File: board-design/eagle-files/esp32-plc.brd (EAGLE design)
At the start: 100 x 80 mm, 42 parts, among them P1 47346-0001, Q1 600mA/40V, Q2 600mA/40V, U1 ESP32-WROOM-32D, U2 FT231XS, U3 BD48E27G-TR, U5 EC20CEFASG-MINIPCIE

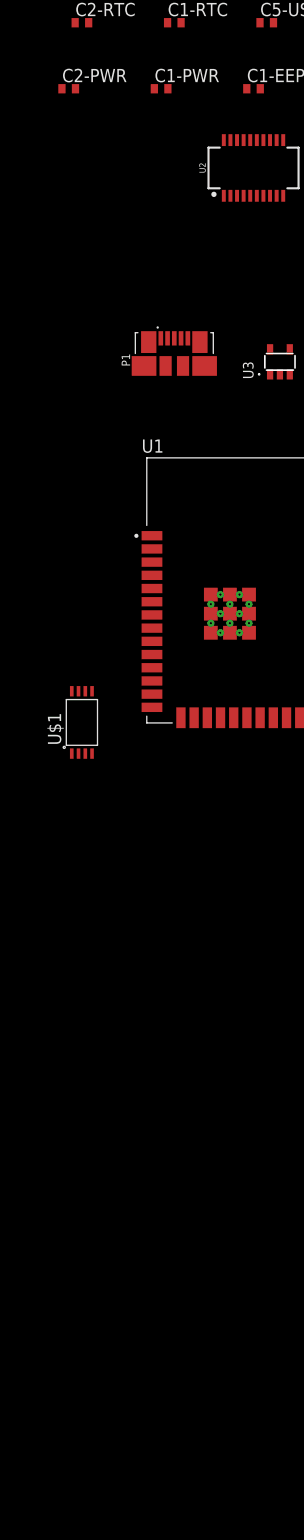
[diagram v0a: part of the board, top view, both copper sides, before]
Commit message: Changed board schematic
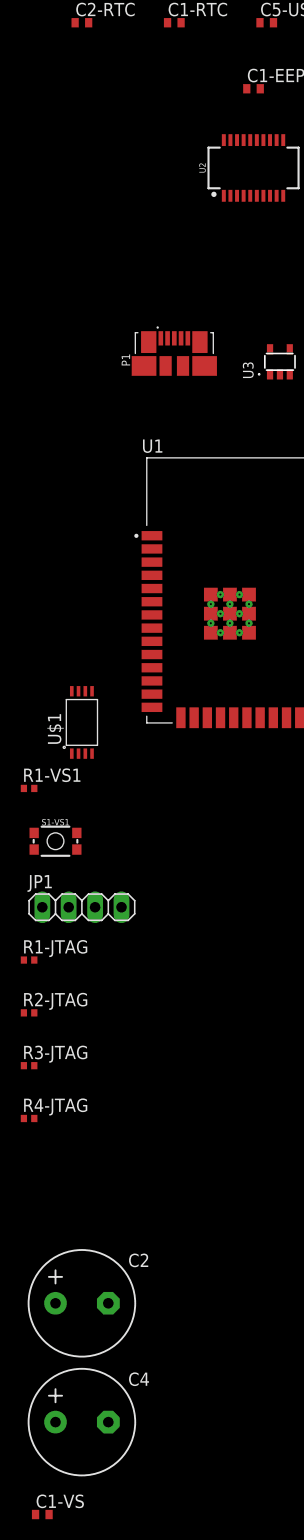
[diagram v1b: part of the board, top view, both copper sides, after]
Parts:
- removed C1-PWR: 100uF, rcl:C0402
- removed C2-PWR: 1000uF, rcl:C0402
- added C1-VS: 47pF, rcl:C0402
- added C2: 1000uF, cap-pan40:E5,0-10
- added C4: 100uF, cap-pan40:E5,0-10
- added JP1: (no value), pinhead:1X04
- added R1-JTAG, R2-JTAG, R3-JTAG, R4-JTAG: 100, rcl:R0402
- added R1-VS1: 10k, rcl:R0402
- added S1-VS1: (no value), SparkFun-Switches:TACTILE_SWITCH_SMD_4.6X2.8MM
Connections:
- net N$14 renamed STATUS
- net N$15 renamed VBAT_BB
- net N$16 renamed VBAT_RF
- net N$17 renamed ANT_DIV
- net N$18 renamed ANT_MAIN
- net N$19 renamed ANT_GNSS
- net N$2 renamed USB_VBUS
- net N$20 renamed ADC0
- net N$21 renamed ADC1
- net N$22 renamed I2C_SDA
- net N$23 renamed I2C_SCL
- net N$24 renamed VDD_EXT
- net N$25 renamed AP_READY
- net N$26 renamed W_DISABLE#
- net N$27 renamed NET_MODE
- net N$28 renamed NET_STATUS
- net N$39 renamed WAKEUP_IN
- net N$40 renamed DBG_RXD
- net N$41 renamed DBG_TXD
- net N$42 renamed USIM_VDD
- net N$43 renamed USIM_GND
- net N$44 renamed USIM_DATA
- net N$45 renamed USIM_CLK
- net N$46 renamed USIM_RST
- net N$47 renamed RESET_IN
- net N$48 renamed PWRKEY
- net N$49 renamed PCM_IN
- net N$5 renamed USB_DM
- net N$50 renamed PCM_OUT
- net N$51 renamed PCM_SYNC
- net N$52 renamed PCM_CLK
- net N$53 renamed RESERVED
- net N$6 renamed USB_DP
- removed net IO18: U1.30
- removed net IO19: U1.31
- removed net IO21: U1.33
- removed net IO22: U1.36
- removed net IO23: U1.37
- removed net IO25: U1.10
- removed net IO26: U1.11
- removed net IO27: U1.12
- removed net IO5: U1.29
- removed net N$54: U5.100, U5.101, U5.102, U5.103, U5.104, U5.105, U5.106, U5.107, U5.108, U5.109, U5.110, U5.111, U5.112, U5.19, U5.22, U5.36, U5.46, U5.48, U5.50, U5.51, U5.52, U5.53, U5.54, U5.56, U5.72, U5.8, U5.85, U5.86, U5.87, U5.88, U5.89, U5.9, U5.90, U5.91, U5.92, U5.93, U5.94, U5.95, U5.96, U5.97, U5.98, U5.99
- new net MTCK: JP1.3, R3-JTAG.2
- new net MTDI: JP1.2, R2-JTAG.2
- new net MTDO: JP1.4, R4-JTAG.2
- new net MTMS: JP1.1, R1-JTAG.2
- new net VIN: C4.+, U$2.1
- net 3V3: now also C1-VS.1, C2.+, R1-VS1.2; no longer C2-PWR.1
- net EEPROM_CLK: now also U1.30
- net EEPROM_CS: now also U1.29
- net EEPROM_DI: now also U1.37
- net EEPROM_DO: now also U1.31
- net EEPROM_HD: now also U1.33
- net EEPROM_WP: now also U1.36
- net GND: now also C1-VS.2, C2.-, C4.-, S1-VS1.3, S1-VS1.4, U5.100, U5.101, U5.102, U5.103, U5.104, U5.105, U5.106, U5.107, U5.108, U5.109, U5.110, U5.111, U5.112, U5.19, U5.22, U5.36, U5.46, U5.48, U5.50, U5.51, U5.52, U5.53, U5.54, U5.56, U5.72, U5.8, U5.85, U5.86, U5.87, U5.88, U5.89, U5.9, U5.90, U5.91, U5.92, U5.93, U5.94, U5.95, U5.96, U5.97, U5.98, U5.99; no longer C1-PWR.2, C2-PWR.2
- net IO0: no longer U1.25
- net IO12: now also R2-JTAG.1
- net IO13: now also R3-JTAG.1
- net IO14: now also R1-JTAG.1
- net IO15: now also R4-JTAG.1
- net N$1: now also R1-VS1.1, S1-VS1.1, S1-VS1.2, U1.25; no longer C1-PWR.1, U$2.1
- net RTC_MFP: now also U1.12
- net SCL: now also U1.10
- net SDA: now also U1.11

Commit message: Eagle schematic changed
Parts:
- removed C1-ESP: 1uF, rcl:C0402
- removed C1-RTC, C2-RTC: 5pF, rcl:C0402
- removed C1-USB, C3, C3-ESP: 0.1uF, rcl:C0402
- removed C2: 1000uF, cap-pan40:E5,0-10
- removed C2-ESP: 10uF, rcl:C0402
- removed C2-USB: 4.7uF, rcl:C0402
- removed C3-USB, C4-USB: 47pF, rcl:C0402
- removed C4: 100uF, cap-pan40:E5,0-10
- removed C5-USB: 10nF, rcl:C0402
- removed JP1: (no value), pinhead:1X04
- removed LED-RX, LED-TX: (no value), adafruit:CHIP-LED0603
- removed P1: 47346-0001, 47346-0001:MOLEX_47346-0001
- removed PFMF.050.2: 500mA, varistor:CT/CN1812
- removed R1-JTAG, R2-JTAG, R3-JTAG, R4-JTAG: 100, rcl:R0402
- removed R1-USB, R2-USB: 330, rcl:R0402
- removed R2-RTC, R3-RTC: 10K, rcl:R0402
- removed R3-USB, R4-USB: 27, rcl:R0402
- removed U1: ESP32-WROOM-32D, ESP32-WROOM-32D:MODULE_ESP32-WROOM-32D
- removed U2: FT231XS, SparkFun-IC-Comms:SSOP20_L
- removed U3: BD48E27G-TR, BD48E27G-TR:SSOP5
- removed U5: EC20CEFASG-MINIPCIE, Quectel:EC20CEFASG
- added C4-RTC: 100pF, rcl:C0402
- added D1: 24V, SparkFun-DiscreteSemi:0603
- added D2, D3: 3A/40V/500mV, SparkFun-DiscreteSemi:SMA-DIODE
- added EERAM-C1, ETH-VDD1A-C2, ETH-VDD2A-C2, ETH-VDDIO-C2, LTE-USIM-C1, LTE-VBAT-C2, LTE-VBAT-C6, PSU-OUT-C6: 100nF, rcl:C0402
- added EERAM-C2: 33uF / 6.3V, rcl:C0402
- added ESP-C1: 22uF, rcl:C0402
- added ESP-C2: 0.1uF, rcl:C0402
- added ESP-C3, ETH-RJ45-C1, ETH-VDDCR-C1: 1uF, rcl:C0402
- added ESP-JTAG: (no value), pinhead:1X04
- added ESP-R5, ESP-R6, ETH-RJ45-R10, ETH-RJ45-R9: 10k, rcl:R0402
- added ESP-UART0: (no value), pinhead:1X06
- added ETH-RJ45-R1, ETH-RJ45-R2, ETH-RJ45-R3, ETH-RJ45-R4: 49.9R, rcl:R0402
- added ETH-RJ45-R5, ETH-RJ45-R6, R1-RTC1: 1k, rcl:R0402
- added ETH-RJ45-R7: 12.1R (1%), rcl:R0402
- added ETH-RJ45-R8: 500R, rcl:R0402
- added ETH-VDD1A-C1, ETH-VDD2A-C1, PSU-IN-C3: 10uF, rcl:C0402
- added ETH-VDD2A-C3, ETH-VDD2A-C4, ETH-VDD2A-C5: 20pF, rcl:C0402
- added ETH-VDDCR-C2: 470pF, rcl:C0402
- added ETH-VDDIO-C1, LTE-VBAT-C10, LTE-VBAT-C9, PSU-OUT-C3: 22uF, rcl:C/6032-28R
- added FB1: 30Ω/1.8A, SparkFun-Coils:0603
- added G1: CR2032H, battery:CR2032H
- added L1: 330uH, rcl:L1812
- added L2, L3, L4: (no value), SparkFun-Coils:XFL4020
- added LTE-USIM-C2, LTE-USIM-C3, LTE-USIM-C4, LTE-VBAT-C3, LTE-VBAT-C7: 33pF, rcl:C0402
- added LTE-USIM-R1: 15K, rcl:R0402
- added LTE-USIM-R2, LTE-USIM-R3, LTE-USIM-R4, PSU-OUT-R1: 0R, rcl:R0402
- added LTE-VBAT-C1, LTE-VBAT-C11, LTE-VBAT-C5, PSU-OUT-C2: 100uF, rcl:C/6032-28R
- added LTE-VBAT-C4, LTE-VBAT-C8: 10pF, rcl:C0402
- added PSU-IN-C1, PSU-IN-C2: 47uF, rcl:C/6032-28R
- added PSU-OUT-C1: 10uF, rcl:C/6032-28R
- added PSU-OUT-C4: 220uF, rcl:C/6032-28R
- added PSU-OUT-C5: 470uF, rcl:C/6032-28R
- added RTC-C2, RTC-C3: 15pF, rcl:C0402
- added U$10: ESDA6V1P6, my-STMicroelectronics:SOT-666
- added U$11: LAN8720A-CP, my-MicrochipTechnology:QFN-24(4X4MM)
- added U$12: 7499010121A, my-WurthElektronik:RJ45-7499010121A
- added U$7: BD48E30G-TR, my-ROHMSemiconductor:SSOP5
- added U$8: LM2576SX-3.3/NOPB, my-Texas-Instruments:TO-263-5
- added U$9: 104224-0820, my-Molex:104224-0820
- added U$93: ECS-250-20-30B-AEN-TR, my-ECSInc:3.2X5MM
- U$1: value M95M01-DWDW3TP/K -> M95M01-DWMN3TP/K; device my-STM:TSSOP-8 -> my-STMicroelectronics:SO8
- U$2: value LM2576HVSX-3.3/NOPB -> ESP32-WROVER-E/IE; device my-TI:TO-263-5 -> my-Espressif-Systems:ESP32-WROVER-E/IE
- U$3: value MCP7940M-I/SN -> MCP7940N-I/SN; device my-Microchip:SOIC-8 -> my-Microchip-Technology:SOIC-8
- U$4: value FC-135-32.7680KA-AG0 -> ECS-.327-12.5-12QS-TR; device my-ET:3.2X1.5MM -> my-ECSInc:2X1.2
- U$5: value V3PM6-M3/H -> 48L512T-I/SN; device my-Vishay:DO-220AA -> my-Microchip-Technology:SOIC-8
- U$6: value SDR1005-101KL -> EC20CEFASG-MINIPCIE; device my-Bourns:SDR1005 -> my-Quectel:EC20-R2.1
- VS-C1: value 47pF -> 1uF
- moved U$5 359.6 mm to (-222.2, -254.0)
- moved U$6 356.8 mm to (-242.6, -252.7)
- moved U$4 355.5 mm to (-214.6, -240.0)
- moved U$3 331.1 mm to (-213.4, -229.9)
- moved U$2 297.3 mm to (-190.5, -201.9)
- moved U$1 267.8 mm to (-204.5, -229.9)
- renumbered C1-EEPROM to EEPROM-C1, C1-VS to VS-C1, C3-RTC to RTC-C1, R1-VS to ESP-R3, R1-VS1 to ESP-R4, R6 to ESP-R2, R7 to ESP-R1, S1-VS to ESP-S1, S1-VS1 to ESP-S2
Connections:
- removed net 3V3: C2-ESP.1, C2.+, C3-ESP.1, EEPROM-C1.1, ESP-R3.2, ESP-R4.2, R1-RTC.2, R2-RTC.2, R2-USB.2, R3-RTC.2, RTC-C1.1, U$1.8, U$2.4, U$3.8, U$6.1, U1.2, U3.2, VS-C1.1
- removed net ADC0: U5.45
- removed net ADC1: U5.44
- removed net ANT_DIV: U5.35
- removed net ANT_GNSS: U5.47
- removed net ANT_MAIN: U5.49
- removed net AP_READY: U5.2
- removed net DBG_RXD: U5.11
- removed net DBG_TXD: U5.12
- removed net DTR#: ESP-R1.1, Q1.3, U2.1
- removed net EEPROM_CLK: U$1.6, U1.30
- removed net EEPROM_CS: U$1.1, U1.29
- removed net EEPROM_DI: U$1.5, U1.37
- removed net EEPROM_DO: U$1.2, U1.31
- removed net EEPROM_HD: U$1.7, U1.33
- removed net EEPROM_WP: U$1.3, U1.36
- removed net EN: C1-ESP.1, ESP-R3.1, ESP-S1.1, ESP-S1.2, Q2.3, U1.3, U3.1
- removed net I2C_SCL: U5.41
- removed net I2C_SDA: U5.42
- removed net IO0: Q1.2
- removed net IO12: R2-JTAG.1, U1.14
- removed net IO13: R3-JTAG.1, U1.16
- removed net IO14: R1-JTAG.1, U1.13
- removed net IO15: R4-JTAG.1, U1.23
- removed net IO16: U1.27
- removed net IO17: U1.28
- removed net IO2: U1.24
- removed net IO32: U1.8
- removed net IO33: U1.9
- removed net IO34: U1.6
- removed net IO35: U1.7
- removed net IO4: U1.26
- removed net MTCK: JP1.3, R3-JTAG.2
- removed net MTDI: JP1.2, R2-JTAG.2
- removed net MTDO: JP1.4, R4-JTAG.2
- removed net MTMS: JP1.1, R1-JTAG.2
- removed net NET_MODE: U5.5
- removed net NET_STATUS: U5.6
- removed net PCM_CLK: U5.27
- removed net PCM_IN: U5.24
- removed net PCM_OUT: U5.25
- removed net PCM_SYNC: U5.26
- removed net PWRKEY: U5.21
- removed net RESERVED: U5.113, U5.114, U5.115, U5.116, U5.13, U5.18, U5.23, U5.28, U5.29, U5.3, U5.30, U5.31, U5.32, U5.33, U5.34, U5.37, U5.38, U5.39, U5.40, U5.43, U5.55
- removed net RESET_IN: U5.20
- removed net RTS#: ESP-R2.1, Q2.2, U2.2
- removed net RXD: U1.34, U2.20
- removed net SCK: U1.20
- removed net SCL: R2-RTC.1, U$3.6, U1.10
- removed net SCS: U1.19
- removed net SDA: R3-RTC.1, U$3.5, U1.11
- removed net SDI: U1.22
- removed net SDO: U1.21
- removed net SHD: U1.17
- removed net STATUS: U5.61
- removed net SWP: U1.18
- removed net TXD: U1.35, U2.4
- removed net USBDM: C3-USB.1, P1.2, R3-USB.1
- removed net USBDP: C4-USB.1, P1.3, R4-USB.1
- removed net USB_DM: U5.70
- removed net USB_DP: U5.69
- removed net USB_VBUS: U5.71
- removed net USIM_GND: U5.10
- removed net USIM_VDD: U5.14
- removed net VBAT_BB: U5.59, U5.60
- removed net VBAT_RF: U5.57, U5.58
- removed net VBUS: C5-USB.1, P1.1, PFMF.050.2.2
- removed net VCC-USB: C1-USB.1, C2-USB.1, PFMF.050.2.1, U2.15
- removed net VDD_EXT: U5.7
- removed net VIN: C4.+, U$2.1
- removed net WAKEUP_IN: U5.1
- removed net W_DISABLE#: U5.4
- new net !ESP_DTR: ESP-R1.1, ESP-UART0.4, Q1.3
- new net !ESP_RST: ESP-UART0.5
- new net !ESP_RTS: ESP-R2.1, Q2.2
- new net 24V: FB1.1
- new net 3.3V: D1.2, EEPROM-C1.1, EERAM-C1.1, ESP-UART0.1, L2.P$1, L3.P$1, L4.P$1, PSU-OUT-C3.+, PSU-OUT-C4.+, PSU-OUT-C5.+, PSU-OUT-C6.1, PSU-OUT-R1.1, R1-RTC.2, RTC-C1.1, U$1.8, U$3.8, U$5.8, U$7.2, VS-C1.1
- new net EERAM_VCAP: EERAM-C2.1, U$5.3
- new net ESP_3V3: ESP-C1.1, ESP-C2.1, ESP-R3.2, ESP-R4.2, ESP-R5.2, ESP-R6.2, L4.P$2, LTE-VBAT-C11.+, U$2.2
- new net ESP_BOOT: ESP-R4.1, ESP-S2.1, ESP-S2.2, Q1.2, U$2.25
- new net ESP_EN: ESP-C3.1, ESP-R3.1, ESP-S1.1, ESP-S1.2, Q2.3, U$2.3, U$7.1
- new net ESP_MTCK: ESP-JTAG.3, U$2.16
- new net ESP_MTDI: ESP-JTAG.2, U$2.14
- new net ESP_MTDO: ESP-JTAG.4, U$2.23
- new net ESP_MTMS: ESP-JTAG.1, U$2.13
- new net ESP_RXD0: ESP-UART0.3, U$2.34
- new net ESP_SCL: ESP-R5.1, U$3.6
- new net ESP_SDA: ESP-R6.1, U$3.5
- new net ESP_TXD0: ESP-UART0.2, U$2.35
- new net ESP_VSPICLK: U$2.30
- new net ESP_VSPICS: U$2.29
- new net ESP_VSPID: U$2.37
- new net ESP_VSPIHD: U$2.33
- new net ESP_VSPIQ: U$2.31
- new net ESP_VSPIWP: U$2.36
- new net ETH_NRST: ETH-RJ45-R9.1, ETH-VDD2A-C5.1, U$11.15
- new net ETH_RJ45_LED1: ETH-RJ45-R5.2, U$11.3
- new net ETH_RJ45_LED2: ETH-RJ45-R10.2, ETH-RJ45-R6.2, U$11.2
- new net ETH_RJ45_RXN: ETH-RJ45-R4.2, U$11.22, U$12.6
- new net ETH_RJ45_RXP: ETH-RJ45-R3.2, U$11.23, U$12.3
- new net ETH_RJ45_TXN: ETH-RJ45-R2.2, U$11.20, U$12.2
- new net ETH_RJ45_TXP: ETH-RJ45-R1.2, U$11.21, U$12.1
- new net ETH_VDD: ETH-RJ45-C1.1, ETH-RJ45-R1.1, ETH-RJ45-R2.1, ETH-RJ45-R3.1, ETH-RJ45-R4.1, ETH-RJ45-R9.2, ETH-VDD1A-C1.1, ETH-VDD1A-C2.1, ETH-VDD2A-C1.1, ETH-VDD2A-C2.1, ETH-VDDIO-C1.+, ETH-VDDIO-C2.1, L2.P$2, U$11.1, U$11.19, U$11.9, U$12.4, U$12.5
- new net ETH_VDDCR: ETH-VDDCR-C1.1, ETH-VDDCR-C2.1, U$11.6
- new net ETH_XTAL1: ETH-VDD2A-C3.1, U$11.5, U$93.1
- new net ETH_XTAL2: ETH-RJ45-R8.1, U$11.4
- new net LTE_CTS: U$6.64
- new net LTE_DBG_RXD: U$6.11
- new net LTE_DBG_TXD: U$6.12
- new net LTE_DCD: U$6.63
- new net LTE_DTR: U$6.66
- new net LTE_RI: U$6.62
- new net LTE_RTS: U$6.65
- new net LTE_RXD: U$6.68
- new net LTE_TXD: U$6.67
- new net LTE_USIM_CLK: LTE-USIM-R3.2, U$6.16
- new net LTE_USIM_DATA: LTE-USIM-R2.2, U$6.15
- new net LTE_USIM_GND: LTE-USIM-C1.1, U$6.10, U$9.G1, U$9.G2, U$9.G3, U$9.G4, U$9.S4
- new net LTE_USIM_RST: LTE-USIM-R4.2, U$6.17
- new net LTE_USIM_VDD: LTE-USIM-C1.2, LTE-USIM-R1.2, U$10.1, U$6.14, U$9.S1
- new net LTE_VBAT: L3.P$2, LTE-VBAT-C1.+, LTE-VBAT-C10.+, LTE-VBAT-C2.1, LTE-VBAT-C3.1, LTE-VBAT-C4.1, LTE-VBAT-C5.+, LTE-VBAT-C6.1, LTE-VBAT-C7.1, LTE-VBAT-C8.1, LTE-VBAT-C9.+
- new net N$14: U$2.12
- new net N$15: U$2.11
- new net N$16: U$2.10
- new net N$17: U$2.9
- new net N$18: U$2.8
- new net N$19: U$2.7
- new net N$2: U$5.6
- new net N$20: U$2.6
- new net N$21: U$5.2
- new net N$22: L1.2, PSU-OUT-C1.+, PSU-OUT-C2.+, PSU-OUT-R1.2, U$8.4
- new net N$23: D3.C, L1.1, U$8.2
- new net N$25: ETH-RJ45-R7.2, U$11.24
- new net N$26: U$11.10
- new net N$27: U$2.26
- new net N$28: U$11.11
- new net N$3: U$1.7
- new net N$39: U$11.7
- new net N$40: U$11.8
- new net N$42: U$11.14
- new net N$44: ETH-RJ45-R8.2, ETH-VDD2A-C4.1, U$93.3
- new net N$5: U$1.5
- new net N$6: D2.C, R1-RTC1.2
- new net RTC_VBAT: C4-RTC.1, R1-RTC.1, R1-RTC1.1, U$3.3
- new net USIM_I/O: LTE-USIM-C2.1, LTE-USIM-R1.1, LTE-USIM-R2.1, U$9.S6
- net GND: now also C4-RTC.2, D1.1, D3.A, EERAM-C1.2, EERAM-C2.2, ESP-C1.2, ESP-C2.2, ESP-C3.2, ESP-UART0.6, ETH-RJ45-C1.2, ETH-RJ45-R10.1, ETH-RJ45-R7.1, ETH-VDD1A-C1.2, ETH-VDD1A-C2.2, ETH-VDD2A-C1.2, ETH-VDD2A-C2.2, ETH-VDD2A-C3.2, ETH-VDD2A-C4.2, ETH-VDD2A-C5.2, ETH-VDDCR-C1.2, ETH-VDDCR-C2.2, ETH-VDDIO-C1.-, ETH-VDDIO-C2.2, G1.-, LTE-USIM-C2.2, LTE-USIM-C3.2, LTE-USIM-C4.2, LTE-VBAT-C1.-, LTE-VBAT-C10.-, LTE-VBAT-C11.-, LTE-VBAT-C2.2, LTE-VBAT-C3.2, LTE-VBAT-C4.2, LTE-VBAT-C5.-, LTE-VBAT-C6.2, LTE-VBAT-C7.2, LTE-VBAT-C8.2, LTE-VBAT-C9.-, PSU-IN-C1.-, PSU-IN-C2.-, PSU-IN-C3.2, PSU-OUT-C1.-, PSU-OUT-C2.-, PSU-OUT-C3.-, PSU-OUT-C4.-, PSU-OUT-C5.-, PSU-OUT-C6.2, RTC-C2.2, RTC-C3.2, U$10.2, U$10.5, U$11.25, U$11.26, U$11.27, U$11.28, U$11.29, U$11.30, U$11.31, U$11.32, U$12.11, U$12.13, U$12.14, U$12.8, U$12.9, U$2.1, U$2.15, U$2.38, U$2.39, U$2.40, U$2.41, U$2.42, U$2.43, U$2.44, U$2.45, U$2.46, U$2.47, U$2.48, U$2.49, U$2.50, U$2.51, U$2.52, U$2.53, U$2.54, U$2.55, U$2.56, U$2.57, U$2.58, U$2.59, U$5.4, U$6.100, U$6.101, U$6.102, U$6.103, U$6.104, U$6.105, U$6.106, U$6.107, U$6.108, U$6.109, U$6.110, U$6.111, U$6.112, U$6.19, U$6.22, U$6.36, U$6.46, U$6.48, U$6.50, U$6.51, U$6.52, U$6.53, U$6.54, U$6.56, U$6.72, U$6.8, U$6.85, U$6.86, U$6.87, U$6.88, U$6.89, U$6.9, U$6.90, U$6.91, U$6.92, U$6.93, U$6.94, U$6.95, U$6.96, U$6.97, U$6.98, U$6.99, U$7.3, U$8.3, U$8.5, U$8.6, U$8.7, U$93.2, U$93.4; no longer C1-ESP.2, C1-RTC.2, C1-USB.2, C2-ESP.2, C2-RTC.2, C2-USB.2, C2.-, C3-ESP.2, C3-USB.2, C3.2, C4-USB.2, C4.-, C5-USB.2, P1.5, P1.SH1, P1.SH2, P1.SH3, P1.SH4, P1.SH5, P1.SH6, U$2.3, U$2.5, U$2.6, U$2.7, U$5.1, U1.1, U1.15, U1.38, U1.39_1, U1.39_10, U1.39_11, U1.39_12, U1.39_13, U1.39_14, U1.39_15, U1.39_16, U1.39_17, U1.39_18, U1.39_19, U1.39_2, U1.39_20, U1.39_21, U1.39_3, U1.39_4, U1.39_5, U1.39_6, U1.39_7, U1.39_8, U1.39_9, U2.16, U2.6, U3.3, U5.100, U5.101, U5.102, U5.103, U5.104, U5.105, U5.106, U5.107, U5.108, U5.109, U5.110, U5.111, U5.112, U5.19, U5.22, U5.36, U5.46, U5.48, U5.50, U5.51, U5.52, U5.53, U5.54, U5.56, U5.72, U5.8, U5.85, U5.86, U5.87, U5.88, U5.89, U5.9, U5.90, U5.91, U5.92, U5.93, U5.94, U5.95, U5.96, U5.97, U5.98, U5.99
- net N$1: now also U$5.7; no longer ESP-R4.1, ESP-S2.1, ESP-S2.2, U1.25
- net N$10: now also U$1.3; no longer U5.65
- net N$11: now also U$5.5; no longer U5.64
- net N$12: now also FB1.2, PSU-IN-C1.+, PSU-IN-C2.+, PSU-IN-C3.1, U$8.1; no longer U5.63
- net N$13: now also U$5.1; no longer U5.62
- net N$31: now also U$2.24; no longer LED-TX.C, U2.17
- net N$32: now also U$11.12; no longer LED-RX.C, U2.10
- net N$33: now also U$11.13; no longer R3-USB.2, U2.12
- net N$34: now also U$11.16; no longer R4-USB.2, U2.11
- net N$35: now also U$11.17; no longer C3.1, U2.13, U2.14, U2.3
- net N$36: now also ETH-RJ45-R5.1, U$12.10; no longer LED-TX.A, R1-USB.1
- net N$37: now also U$11.18; no longer LED-RX.A, R2-USB.1
- net N$38: now also ETH-RJ45-R6.1, U$12.12; no longer R1-USB.2
- net N$4: now also U$1.6; no longer U$2.2, U$5.2, U$6.2
- net N$7: now also D2.A, G1.+; no longer U5.68
- net N$8: now also U$1.1; no longer U5.67
- net N$9: now also U$1.2; no longer U5.66
- net RTC_MFP: no longer R1-RTC.1, U1.12
- net RTC_X1: now also RTC-C2.1, U$4.1; no longer C1-RTC.1, U$4.2
- net RTC_X2: now also RTC-C3.1, U$4.2; no longer C2-RTC.1, U$4.1
- net SENSOR_VN: now also U$2.5; no longer U1.5
- net SENSOR_VP: now also U$2.4; no longer U1.4
- net USIM_CLK: now also LTE-USIM-C3.1, LTE-USIM-R3.1, U$10.4, U$9.S3; no longer U5.16
- net USIM_DATA: now also U$10.6; no longer U5.15
- net USIM_RST: now also LTE-USIM-C4.1, LTE-USIM-R4.1, U$10.3, U$9.S2; no longer U5.17

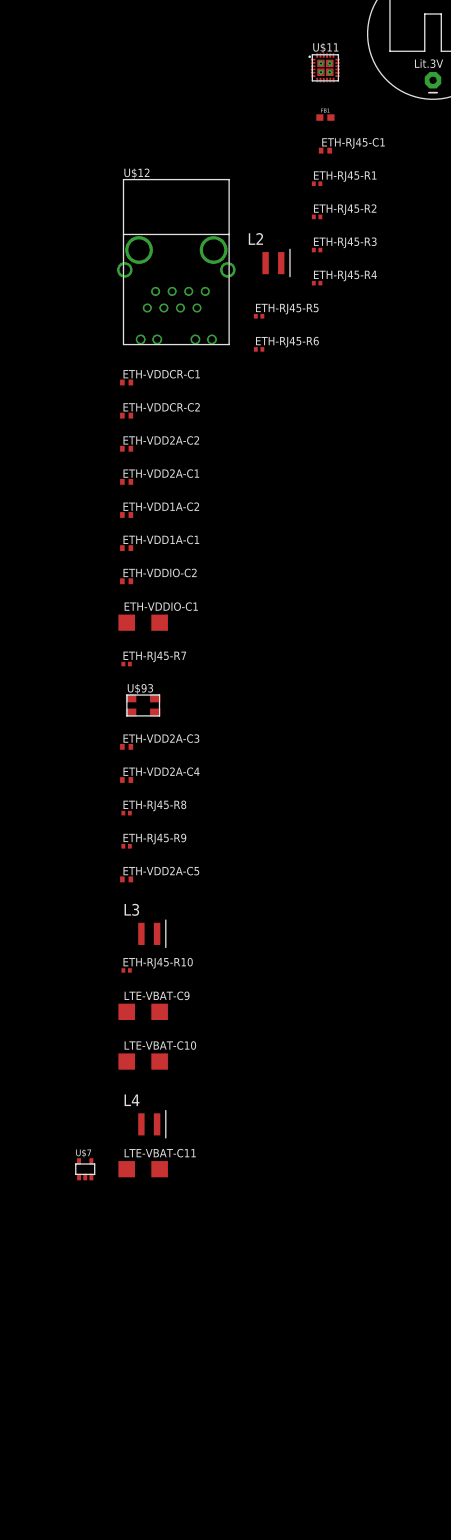
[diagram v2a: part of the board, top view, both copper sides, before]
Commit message: Added RS485 Interface Module
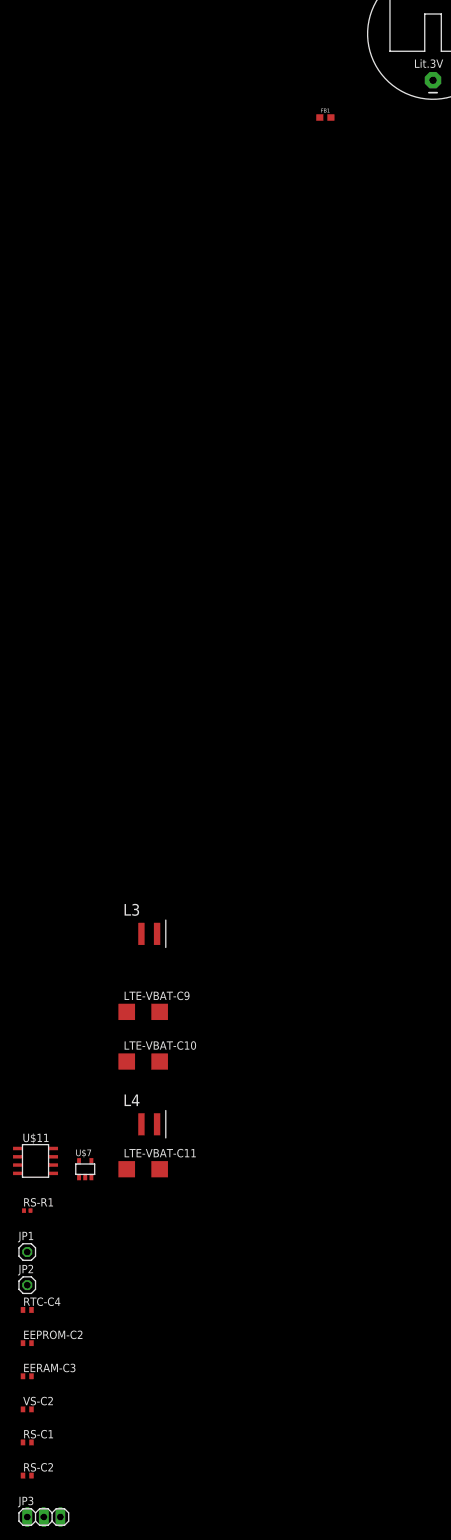
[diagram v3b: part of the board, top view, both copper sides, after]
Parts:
- removed ETH-RJ45-C1, ETH-VDDCR-C1: 1uF, rcl:C0402
- removed ETH-RJ45-R1, ETH-RJ45-R2, ETH-RJ45-R3, ETH-RJ45-R4: 49.9R, rcl:R0402
- removed ETH-RJ45-R10, ETH-RJ45-R9: 10k, rcl:R0402
- removed ETH-RJ45-R5, ETH-RJ45-R6: 1k, rcl:R0402
- removed ETH-RJ45-R7: 12.1R (1%), rcl:R0402
- removed ETH-RJ45-R8: 500R, rcl:R0402
- removed ETH-VDD1A-C1, ETH-VDD2A-C1: 10uF, rcl:C0402
- removed ETH-VDD1A-C2, ETH-VDD2A-C2, ETH-VDDIO-C2: 100nF, rcl:C0402
- removed ETH-VDD2A-C3, ETH-VDD2A-C4, ETH-VDD2A-C5: 20pF, rcl:C0402
- removed ETH-VDDCR-C2: 470pF, rcl:C0402
- removed ETH-VDDIO-C1: 22uF, rcl:C/6032-28R
- removed L2: (no value), SparkFun-Coils:XFL4020
- removed U$12: 7499010121A, my-WurthElektronik:RJ45-7499010121A
- removed U$93: ECS-250-20-30B-AEN-TR, my-ECSInc:3.2X5MM
- added EEPROM-C2, EERAM-C3, RS-C1, RTC-C4, VS-C2: 10uF, rcl:C0402
- added JP1, JP2: (no value), pinhead:1X01
- added JP3: (no value), pinhead:1X03
- added RS-C2: 100nF, rcl:C0402
- added RS-R1: 120, rcl:R0402
- ESP-C2: value 0.1uF -> 100nF
- U$11: value LAN8720A-CP -> MAX3485CSA+T; device my-MicrochipTechnology:QFN-24(4X4MM) -> my-MaximIntegrated:SOIC-8
- VS-C1: value 1uF -> 100nF
- moved U$11 173.4 mm to (-373.4, -660.4)
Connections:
- net N$1 renamed EERAM_HOLD
- net N$10 renamed EEPROM_W
- net N$11 renamed EERAM_SI
- net N$13 renamed EERAM_CS
- net N$2 renamed EERAM_SCK
- net N$21 renamed EERAM_SO
- net N$3 renamed EEPROM_HOLD
- net N$4 renamed EEPROM_C
- net N$5 renamed EEPROM_D
- net N$8 renamed EEPROM_S
- net N$9 renamed EEPROM_Q
- removed net ETH_NRST: ETH-RJ45-R9.1, ETH-VDD2A-C5.1, U$11.15
- removed net ETH_RJ45_LED1: ETH-RJ45-R5.2, U$11.3
- removed net ETH_RJ45_LED2: ETH-RJ45-R10.2, ETH-RJ45-R6.2, U$11.2
- removed net ETH_RJ45_RXN: ETH-RJ45-R4.2, U$11.22, U$12.6
- removed net ETH_RJ45_RXP: ETH-RJ45-R3.2, U$11.23, U$12.3
- removed net ETH_RJ45_TXN: ETH-RJ45-R2.2, U$11.20, U$12.2
- removed net ETH_RJ45_TXP: ETH-RJ45-R1.2, U$11.21, U$12.1
- removed net ETH_VDD: ETH-RJ45-C1.1, ETH-RJ45-R1.1, ETH-RJ45-R2.1, ETH-RJ45-R3.1, ETH-RJ45-R4.1, ETH-RJ45-R9.2, ETH-VDD1A-C1.1, ETH-VDD1A-C2.1, ETH-VDD2A-C1.1, ETH-VDD2A-C2.1, ETH-VDDIO-C1.+, ETH-VDDIO-C2.1, L2.P$2, U$11.1, U$11.19, U$11.9, U$12.4, U$12.5
- removed net ETH_VDDCR: ETH-VDDCR-C1.1, ETH-VDDCR-C2.1, U$11.6
- removed net ETH_XTAL1: ETH-VDD2A-C3.1, U$11.5, U$93.1
- removed net ETH_XTAL2: ETH-RJ45-R8.1, U$11.4
- removed net N$32: U$11.12
- removed net N$33: U$11.13
- removed net N$34: U$11.16
- removed net N$35: U$11.17
- removed net N$36: ETH-RJ45-R5.1, U$12.10
- removed net N$37: U$11.18
- removed net N$38: ETH-RJ45-R6.1, U$12.12
- removed net N$39: U$11.7
- removed net N$40: U$11.8
- removed net N$42: U$11.14
- removed net N$44: ETH-RJ45-R8.2, ETH-VDD2A-C4.1, U$93.3
- new net N$24: U$3.6
- new net P$1: JP3.3
- new net RS-DE: U$11.3
- new net RS-DI: U$11.4
- new net RS-RE: U$11.2
- new net RS-RO: U$11.1
- new net V_IN: JP3.1
- net 3.3V: now also EEPROM-C2.1, EERAM-C3.1, RS-C1.1, RS-C2.1, RTC-C4.1, U$11.8, VS-C2.1; no longer L2.P$1
- net ESP_SCL: no longer U$3.6
- net ESP_SDA: no longer U$3.5
- net GND: now also EEPROM-C2.2, EERAM-C3.2, JP3.2, RS-C1.2, RS-C2.2, RTC-C4.2, U$11.5, VS-C2.2; no longer ETH-RJ45-C1.2, ETH-RJ45-R10.1, ETH-RJ45-R7.1, ETH-VDD1A-C1.2, ETH-VDD1A-C2.2, ETH-VDD2A-C1.2, ETH-VDD2A-C2.2, ETH-VDD2A-C3.2, ETH-VDD2A-C4.2, ETH-VDD2A-C5.2, ETH-VDDCR-C1.2, ETH-VDDCR-C2.2, ETH-VDDIO-C1.-, ETH-VDDIO-C2.2, U$11.25, U$11.26, U$11.27, U$11.28, U$11.29, U$11.30, U$11.31, U$11.32, U$12.11, U$12.13, U$12.14, U$12.8, U$12.9, U$93.2, U$93.4
- net LTE_VBAT: now also U$6.57, U$6.58, U$6.59, U$6.60
- net N$25: now also U$3.5; no longer ETH-RJ45-R7.2, U$11.24
- net N$26: now also JP1.1, RS-R1.1, U$11.7; no longer U$11.10
- net N$28: now also JP2.1, RS-R1.2, U$11.6; no longer U$11.11

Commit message: Updated schematic
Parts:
- removed JP1, JP2: (no value), pinhead:1X01
- added C1: 1nF/1kV, rcl:C0805
- added D4: Green, SparkFun-LED:LED-0603
- added D5: 36V, SparkFun-DiscreteSemi:SOD-323
- added D6: 0.5A/40V/420mV, SparkFun-DiscreteSemi:SOD-323
- added F1: 750mA, adafruit:R1206
- added JP4: (no value), pinhead:1X02
- added LTE-UART-R1, LTE-UART-R10, LTE-UART-R4, LTE-UART-R6, LTE-UART-R8, PSU-OUT-R3: 10K, rcl:R0402
- added LTE-UART-R2, LTE-UART-R3, LTE-UART-R5, LTE-UART-R7, LTE-UART-R9: 4.7K, rcl:R0402
- added LTE-VBAT-C12, LTE-VBAT-C13, LTE-VBAT-C14, LTE-VBAT-C15, LTE-VBAT-C16: 1nF, rcl:C0402
- added PSU-OUT-R2: 330, rcl:R0402
- added PSU-OUT-R4: 1K, rcl:R0402
- added Q3, Q4, Q5, Q6, Q7, Q8: 500mA/300V, SparkFun-DiscreteSemi:SOT23-3
- added R1: 42/2kV, rcl:R0805
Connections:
- removed net LTE_CTS: U$6.64
- removed net LTE_DCD: U$6.63
- removed net LTE_RTS: U$6.65
- removed net N$26: JP1.1, RS-R1.1, U$11.7
- removed net V_IN: JP3.1
- new net LTE_AP_READY: LTE-UART-R10.1, Q7.3, U$6.2
- new net LTE_VDD_EXT: LTE-UART-R1.2, LTE-UART-R10.2, LTE-UART-R2.2, LTE-UART-R3.2, LTE-UART-R5.2, LTE-UART-R6.2, LTE-UART-R7.2, LTE-UART-R9.2, LTE-VBAT-C12.2, LTE-VBAT-C13.2, LTE-VBAT-C14.2, LTE-VBAT-C15.2, LTE-VBAT-C16.2, U$6.7
- new net MCU_EINT: LTE-UART-R8.1, Q6.3
- new net MCU_GPIO0: Q5.2
- new net MCU_GPIO1: Q7.2
- new net MCU_RXD: LTE-UART-R4.1, Q4.3
- new net MCU_TXD: Q3.2
- new net N$1: LTE-UART-R5.1, LTE-VBAT-C14.1, Q5.1
- new net N$10: F1.2, JP3.2
- new net N$11: LTE-UART-R7.1, LTE-VBAT-C15.1, Q6.1
- new net N$13: D6.A, F1.1
- new net N$2: LTE-UART-R2.1, LTE-VBAT-C12.1, Q3.1
- new net N$3: LTE-UART-R3.1, LTE-VBAT-C13.1, Q4.1
- new net N$32: JP4.1, RS-R1.1, U$11.7
- new net N$4: D4.C, Q8.3
- new net N$5: D4.A, PSU-OUT-R2.2
- new net N$8: LTE-UART-R9.1, LTE-VBAT-C16.1, Q7.1
- new net N$9: PSU-OUT-R3.2, PSU-OUT-R4.1, Q8.1
- new net PSU_PWR_LED: PSU-OUT-R4.2
- net 24V: now also D5.C, D6.C
- net 3.3V: now also LTE-UART-R4.2, LTE-UART-R8.2, PSU-OUT-R2.1, PSU-OUT-R3.1
- net GND: now also C1.1, D5.A, JP3.3, Q8.2, R1.2; no longer JP3.2
- net LTE_DTR: now also LTE-UART-R6.1, Q5.3
- net LTE_RI: now also Q6.2
- net LTE_RXD: now also LTE-UART-R1.1, Q3.3
- net LTE_TXD: now also Q4.2
- net N$28: now also JP4.2; no longer JP2.1
- net P$1: now also C1.2, JP3.1, R1.1; no longer JP3.3

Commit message: Logic unit schematic updated
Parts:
- removed ESP-JTAG: (no value), pinhead:1X04
- removed ESP-UART0: (no value), pinhead:1X06
- added JP1: (no value), pinhead:2X03
- added JP2: (no value), pinhead:2X05
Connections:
- removed net !ESP_DTR: ESP-R1.1, ESP-UART0.4, Q1.3
- removed net !ESP_RST: ESP-UART0.5
- removed net !ESP_RTS: ESP-R2.1, Q2.2
- removed net EEPROM_C: U$1.6
- removed net EEPROM_D: U$1.5
- removed net EEPROM_HOLD: U$1.7
- removed net EEPROM_Q: U$1.2
- removed net EEPROM_S: U$1.1
- removed net EEPROM_W: U$1.3
- removed net EERAM_CS: U$5.1
- removed net EERAM_HOLD: U$5.7
- removed net EERAM_SCK: U$5.6
- removed net EERAM_SI: U$5.5
- removed net EERAM_SO: U$5.2
- removed net ESP_MTCK: ESP-JTAG.3, U$2.16
- removed net ESP_MTDI: ESP-JTAG.2, U$2.14
- removed net ESP_MTDO: ESP-JTAG.4, U$2.23
- removed net ESP_MTMS: ESP-JTAG.1, U$2.13
- removed net ESP_VSPICS: U$2.29
- removed net N$14: U$2.12
- removed net N$15: U$2.11
- removed net N$16: U$2.10
- removed net N$17: U$2.9
- removed net N$18: U$2.8
- removed net N$19: U$2.7
- removed net N$20: U$2.6
- removed net N$24: U$3.6
- removed net N$25: U$3.5
- removed net N$27: U$2.26
- removed net N$31: U$2.24
- new net !ESP_DTR0: ESP-R1.1, JP1.2, Q1.3
- new net !ESP_RTS0: ESP-R2.1, JP1.4, Q2.2
- new net ESP_HSPICLK: JP2.5, U$2.13
- new net ESP_HSPICS0: JP2.3, U$2.23
- new net ESP_HSPID: JP2.6, U$2.16
- new net ESP_HSPIHD: JP2.4, U$2.26
- new net ESP_HSPIINT: JP2.2, U$2.8
- new net ESP_HSPIQ: JP2.7, U$2.14
- new net ESP_HSPIWP: JP2.9, U$2.24
- new net ESP_VSPICS0: U$1.1, U$2.29
- new net ESP_VSPICS1: U$2.12, U$5.1
- net 3.3V: now also JP1.1, JP2.1; no longer ESP-UART0.1
- net ESP_RXD0: now also JP1.5; no longer ESP-UART0.3
- net ESP_SCL: now also U$2.10, U$3.6
- net ESP_SDA: now also U$2.11, U$3.5
- net ESP_TXD0: now also JP1.3; no longer ESP-UART0.2
- net ESP_VSPICLK: now also U$1.6, U$5.6
- net ESP_VSPID: now also U$1.2, U$5.2
- net ESP_VSPIHD: now also U$1.7, U$5.7
- net ESP_VSPIQ: now also U$1.5, U$5.5
- net ESP_VSPIWP: now also U$1.3
- net GND: now also JP1.6, JP2.10, JP2.8; no longer ESP-UART0.6
- net RTC_MFP: now also U$2.9
